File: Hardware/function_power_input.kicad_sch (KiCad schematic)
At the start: 51 parts, among them J2 USB_C_Receptacle_USB2.0_14P, Q1 NMOS, U2 AZ1117-3.3, U3 IP2721, U5 AZ1117D-ADJ, U7 AZ1117-5.0

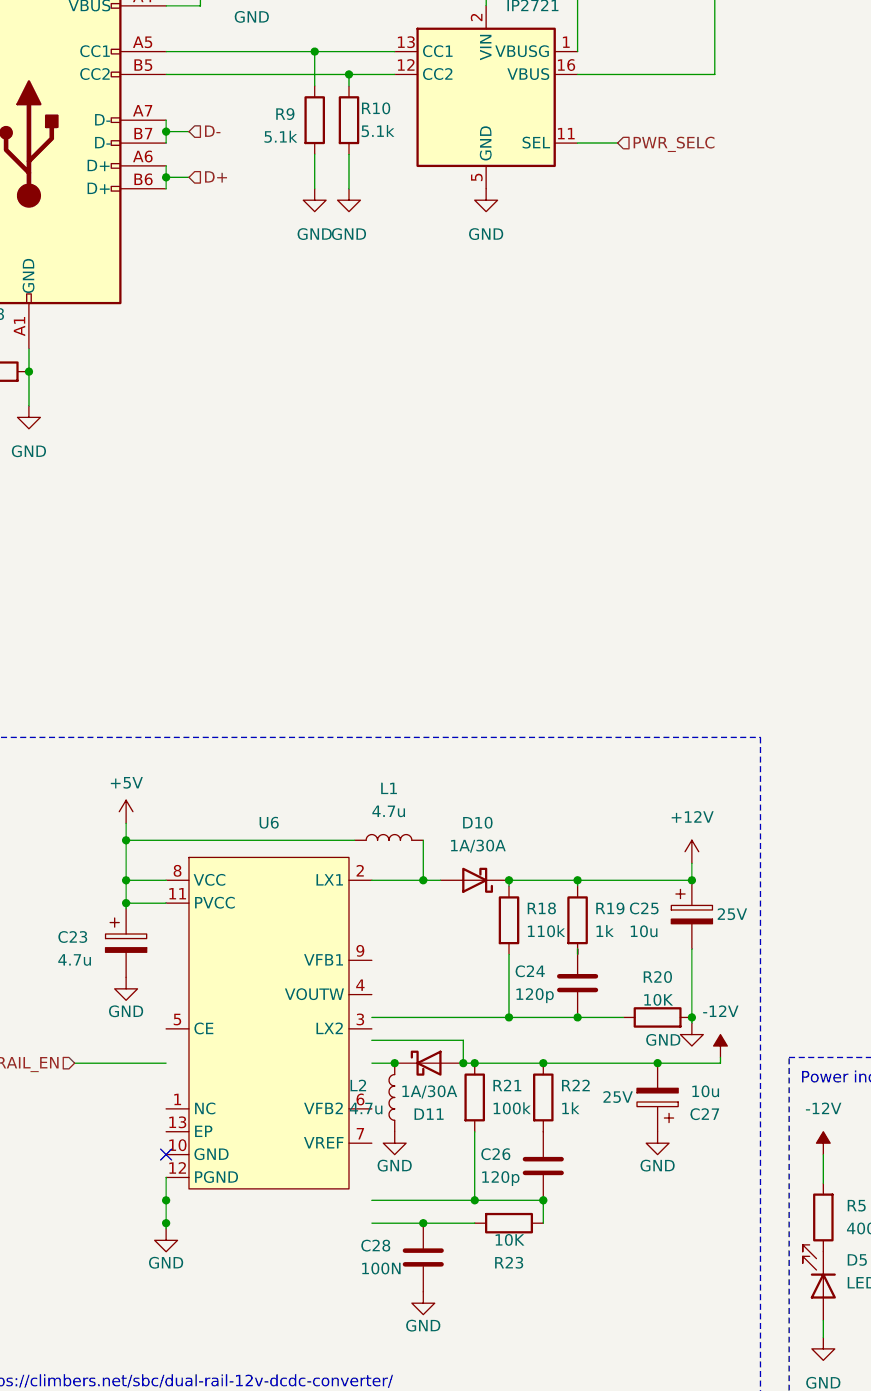
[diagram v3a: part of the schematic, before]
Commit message: Added docs for power select pins
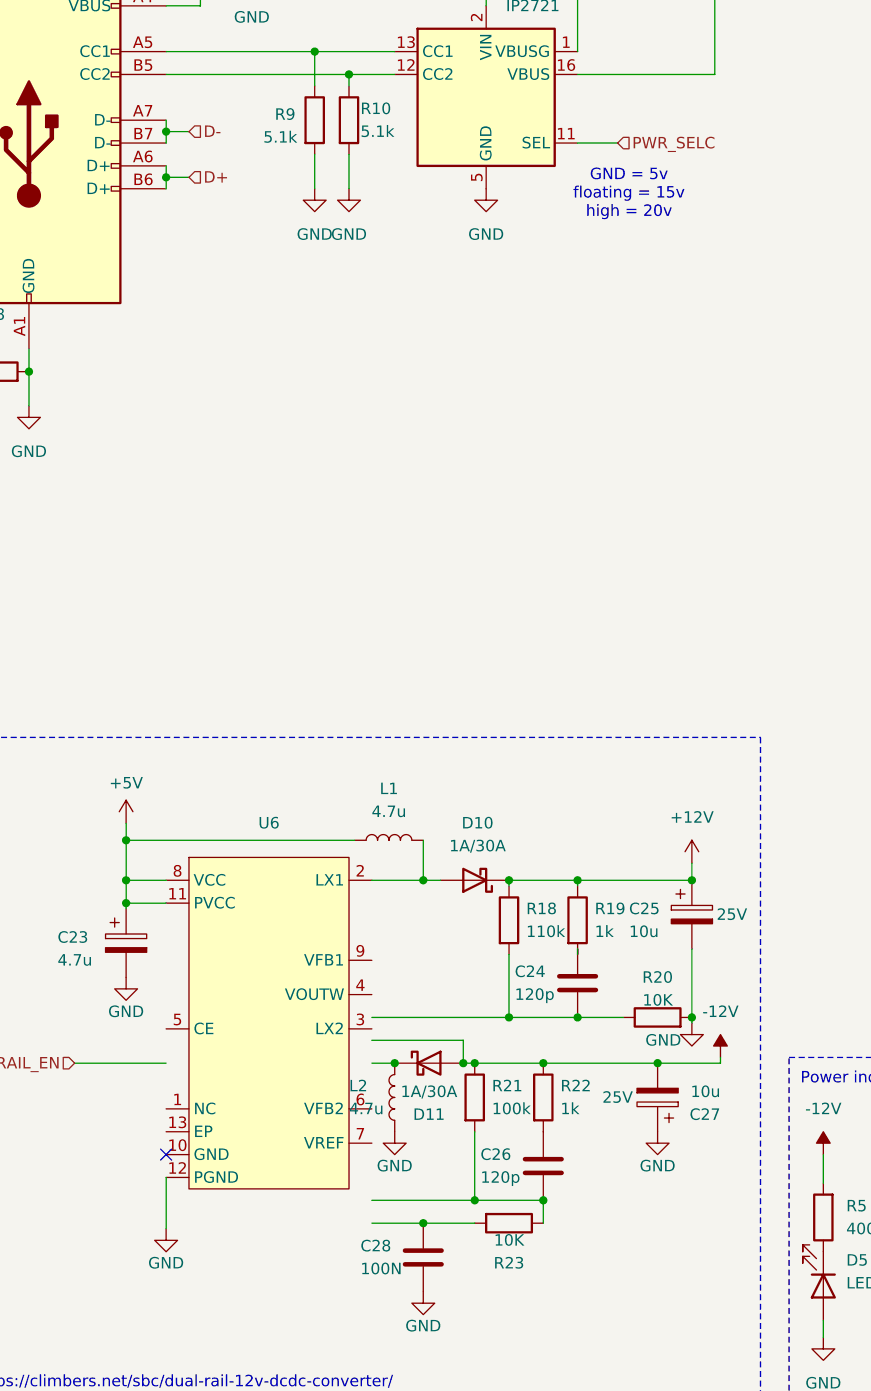
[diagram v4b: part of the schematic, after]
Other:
- note added: "GND = 5v floating = 15v high = 20v"
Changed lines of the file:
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@@
-	)
-	(junction
-		(at 42.545 175.26)
-		(diameter 0)
-		(color 0 0 0 0)
-	)
-	(junction
-		(at 42.545 172.72)
-		(diameter 0)
-		(color 0 0 0 0)
 	)
 	(junction
@@
 	(wire
 		(pts
-			(xy 42.545 172.72) (xy 42.545 175.26)
-		)
-		(stroke
-			(width 0)
-			(type default)
-		)
-	)
-	(wire
-		(pts
 			(xy 88.265 47.625) (xy 103.505 47.625)
 		)
@@
 	(wire
 		(pts
-			(xy 42.545 175.26) (xy 42.545 175.895)
-		)
-		(stroke
-			(width 0)
-			(type default)
-		)
-	)
-	(wire
-		(pts
 			(xy 84.455 157.48) (xy 97.155 157.48)
 		)
@@
 	(wire
 		(pts
-			(xy 42.545 170.18) (xy 42.545 172.72)
+			(xy 42.545 170.18) (xy 42.545 175.895)
 		)
 		(stroke
@@
 		(effects
 			(font
+				(size 1.27 1.27)
+			)
+		)
+	)
+	(text "GND = 5v\nfloating = 15v\nhigh = 20v"
+		(exclude_from_sim no)
+		(at 93.98 60.96 0)
+		(effects
+			(font
